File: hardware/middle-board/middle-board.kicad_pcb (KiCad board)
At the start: 4 copper layers, 39 x 110 mm, 69 parts, among them J1 Conn_01x10_Socket, J2 Conn_01x15_Socket, J3 Conn_01x10_Pin, J4 Conn_01x09_Socket, J5 Conn_01x09_Socket, J6 Conn_01x12_Pin, Q1 2N3904, Q2 2N3906, Q3 2N3904, Q4 2N3906, U1 TL084, U2 TL074, U3 TL072, U4 NE5517

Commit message: wip - first pass done
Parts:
- C10, C3, C4, C5, C6, C7, C8, C9: footprint Capacitor_THT:C_Disc_D3.4mm_W2.1mm_P2.50mm -> Eurorack Common:C_Disc_D3.4mm_W2.1mm_P2.50mm
- Q1, Q2, Q3, Q4: footprint Package_TO_SOT_THT:TO-92_Inline -> Eurorack Common:TO-92_Inline
- R1, R10, R11, R12, R13, R14, R15, R16, R17, R18, R19, R2, R20, R21, R22, R23, R24, R25, R26, R27, R28, R29, R3, R30, R31, R32, R33, R34, R35, R36, R37, R38, R39, R4, R40, R41, R42, R43, R5, R6, R7, R8, R9: footprint Resistor_THT:R_Axial_DIN0207_L6.3mm_D2.5mm_P7.62mm_Horizontal -> Eurorack Common:R_Axial_DIN0207_L6.3mm_D2.5mm_P7.62mm_Horizontal
- U2: footprint Package_DIP:DIP-14_W7.62mm -> Eurorack Common:DIP-14_W7.62mm
- U3: footprint Package_DIP:DIP-8_W7.62mm -> Eurorack Common:DIP-8_W7.62mm
- U4: footprint Package_SO:JEITA_SOIC-16_3.9x9.9mm_P1.27mm -> Eurorack Common:SOIC-16_3.9x9.9mm_P1.27mm

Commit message: chore: clean up the boards
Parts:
- J1: value Conn_01x10_Socket -> 01x10 Male Pin Header
- J2: value Conn_01x15_Socket -> 01x13 Female Pin Header
- J3: value Conn_01x10_Pin -> 01x10 Male Pin Header
- J4, J5: value Conn_01x09_Socket -> 01x09 Female Pin Header
- J6: value Conn_01x12_Pin -> 01x12 Female Pin Header
- RV1, RV3: value 2K -> B2K
- RV2, RV4: value 100K -> B100K

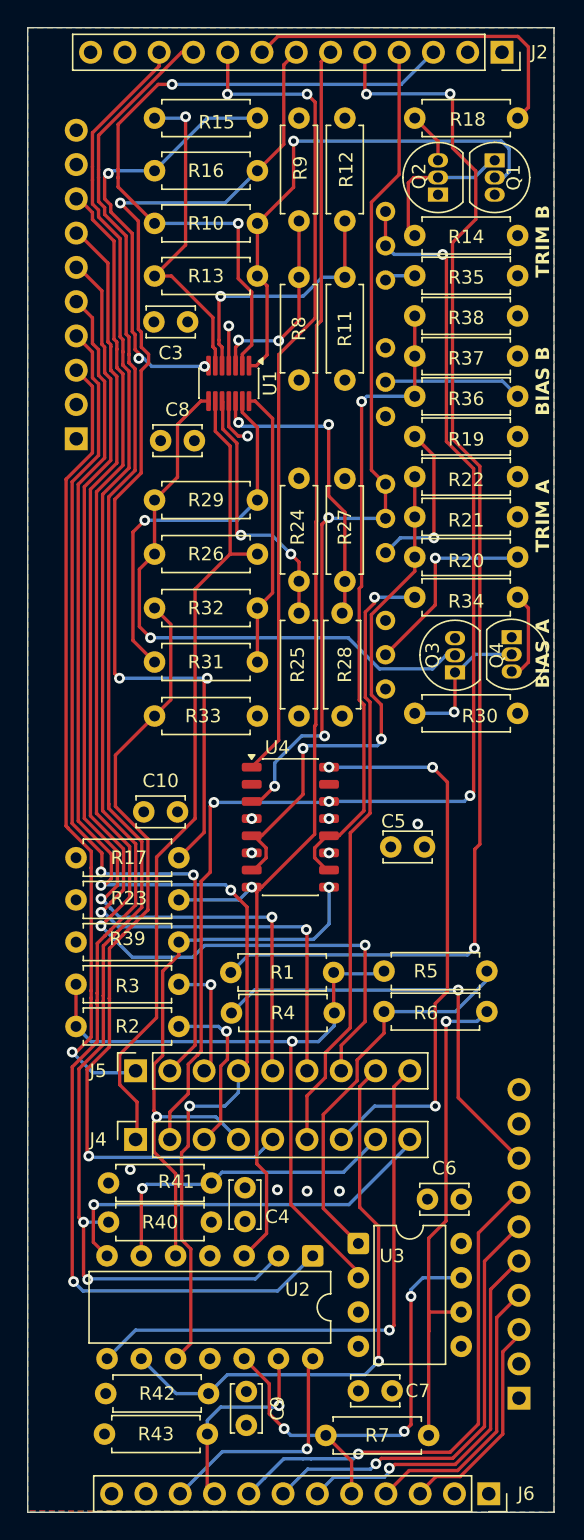
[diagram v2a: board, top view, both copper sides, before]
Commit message: feature: optional DIP footprint on PCB for TL0X4 op amps
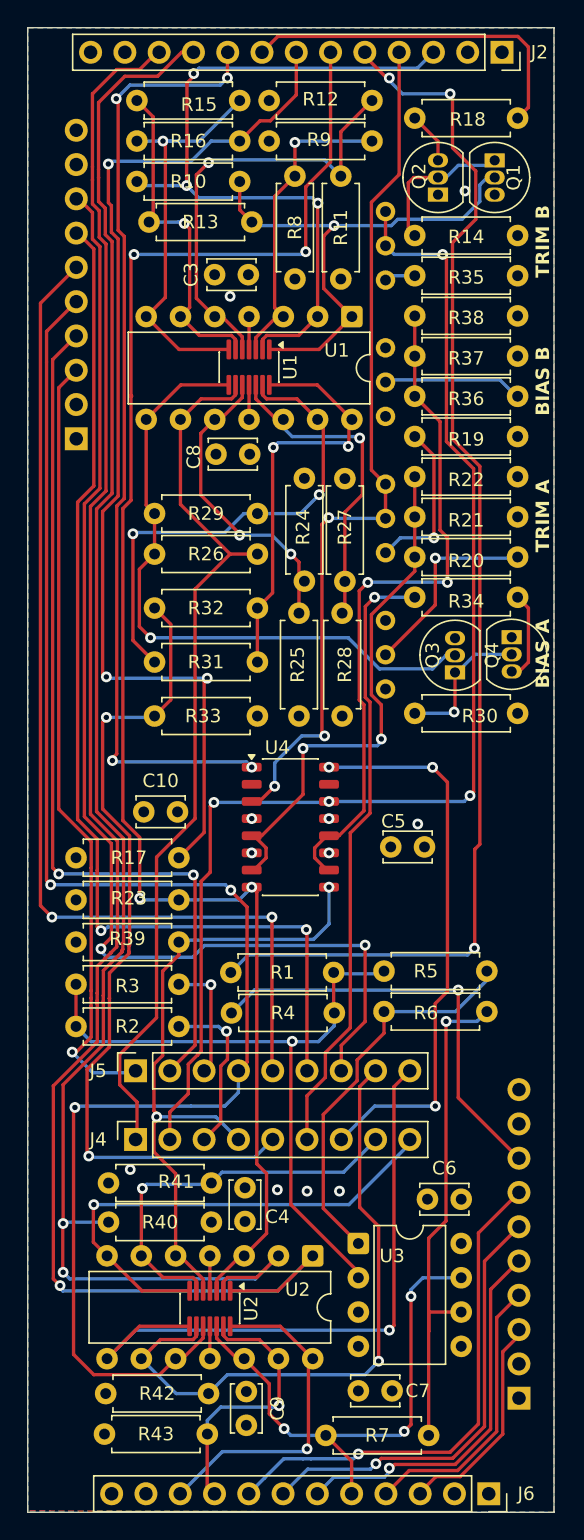
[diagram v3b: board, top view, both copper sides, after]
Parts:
- added U1: TL084, Eurorack Common:DIP-14_W7.62mm, F.Cu at (44.0, 41.4)
- added U2: TL074, Eurorack Common:Texas_DYY0014A_TSOT-23-14_2x4.2mm_P0.5mm, F.Cu at (33.5, 114.9)
- moved R9 8.02 mm to (45.5, 28.4), turned to 180 degrees
- moved R11 7.50 mm to (43.2, 31.0)
- moved R8 7.50 mm to (39.8, 38.6)
- moved R12 5.76 mm to (37.9, 25.4), turned to 0 degrees
- moved C3 5.70 mm to (36.4, 38.3)
- moved C8 4.22 mm to (34.0, 51.6)
- moved R13 4.02 mm to (36.6, 34.4)
- moved R10 3.37 mm to (28.1, 31.4)
- moved R16 2.56 mm to (28.1, 28.4)
- moved U1 1.92 mm to (36.4, 45.2)
- moved R15 1.85 mm to (35.7, 25.4)
- moved R29 1.00 mm to (29.4, 56.0)
- moved R24 0.40 mm to (40.5, 53.4)
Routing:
- net /OUT_C: track 95.7 -> 116.6 mm
- net /OUT_A: track 99.0 -> 117.7 mm, vias 1 -> 4
- net Net-(U1B-+): track 19.2 -> 32.9 mm
- net Net-(R31-Pad1): track 20.8 -> 31.5 mm, vias 0 -> 2
- net /COMMON_A: track 61.1 -> 71.0 mm, vias 2 -> 4
- net /LED_A2: track 117.2 -> 125.7 mm
- net Net-(U1D--): track 28.3 -> 36.6 mm, vias 1 -> 2
- net /LED_A1: track 116.4 -> 124.7 mm
- net Net-(U1A-+): track 15.2 -> 23.1 mm, vias 2 -> 1
- net /LED_B2: track 29.8 -> 37.0 mm
- net /LED_C2: track 41.6 -> 48.8 mm
- net /LED_MIX2: track 17.6 -> 24.7 mm
- net /LED_B1: track 23.8 -> 29.4 mm
- net /LED_C1: track 42.2 -> 47.7 mm
- net /LED_MIX1: track 14.9 -> 20.4 mm
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
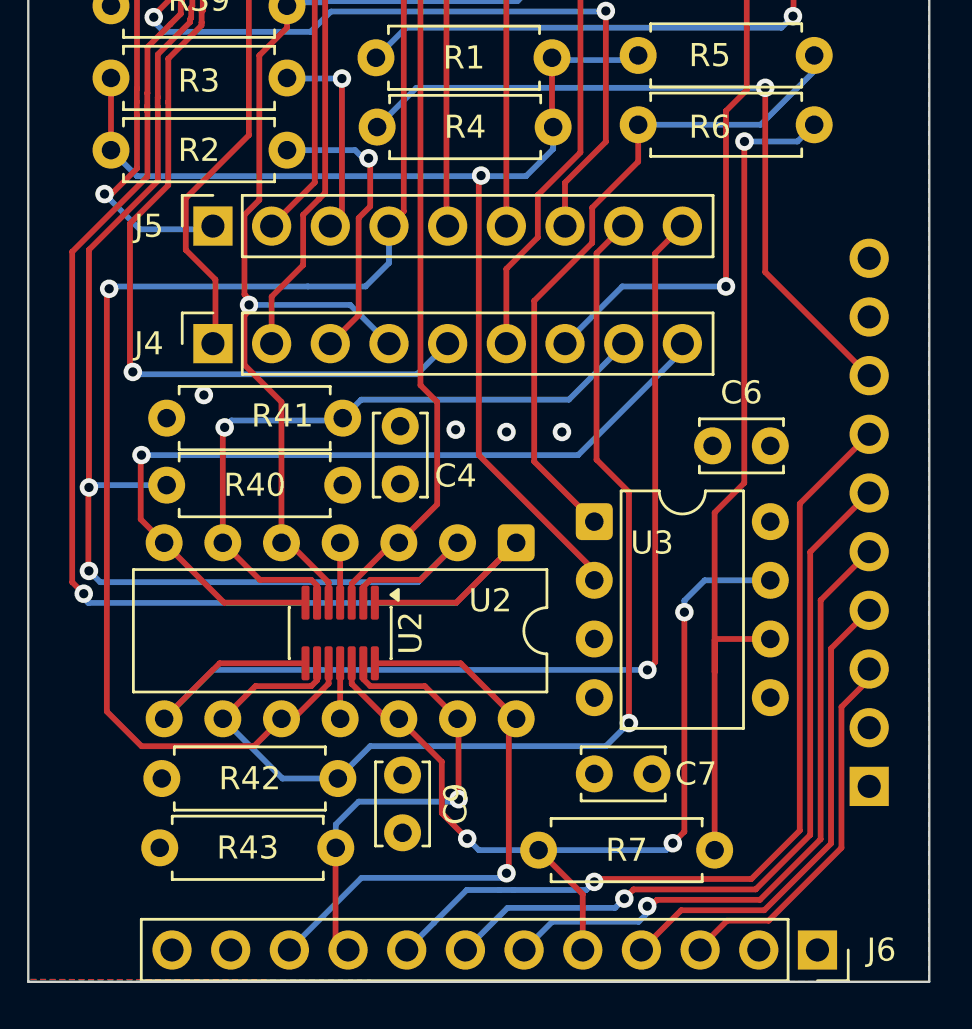
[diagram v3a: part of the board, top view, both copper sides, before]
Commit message: fix: inverted power pins on op amps
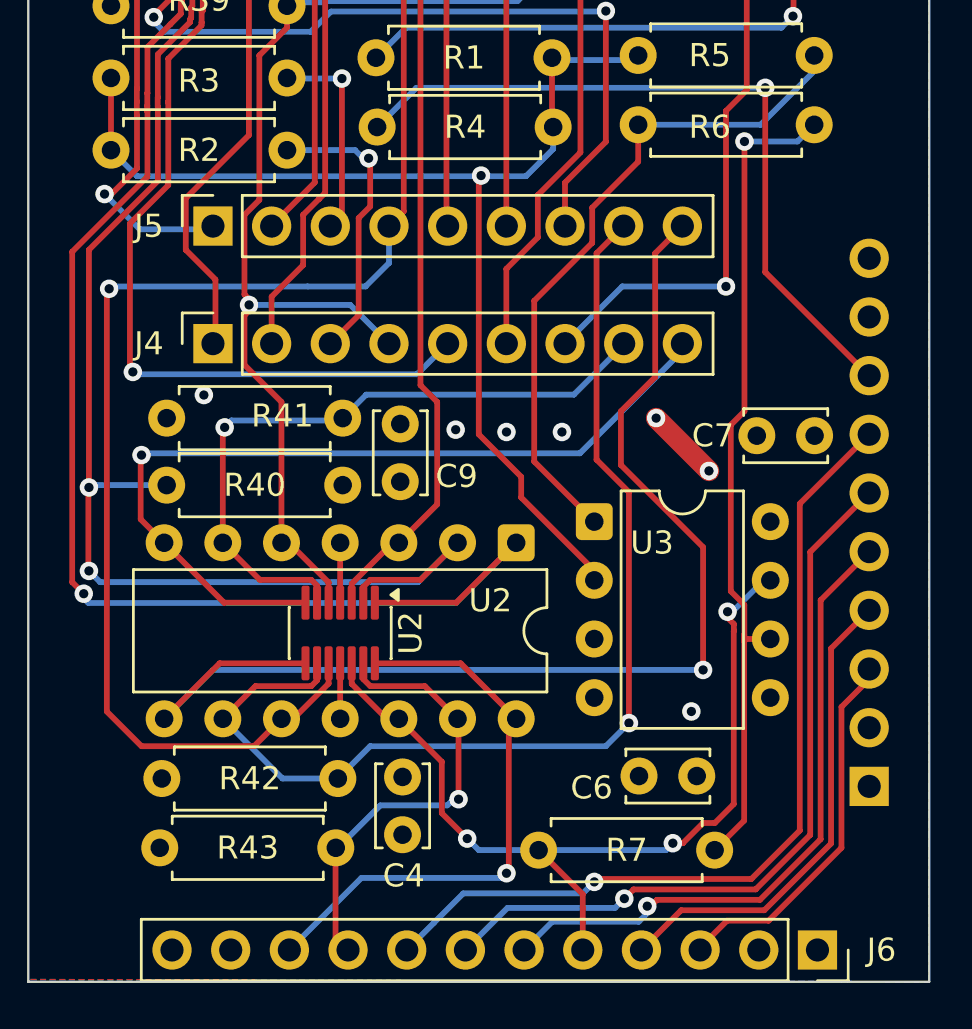
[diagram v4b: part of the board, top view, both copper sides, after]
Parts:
- moved C7 17.5 mm to (54.0, 106.4), turned to 180 degrees
- moved C6 14.3 mm to (48.9, 121.1), turned to 180 degrees
- moved C4 2.58 mm to (36.2, 123.6), turned to 90 degrees
- moved C9 2.40 mm to (36.1, 108.4), turned to 90 degrees
- renumbered C9 to C4, C4 to C9
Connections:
- C4 pad 1: +12V -> GND
- C4 pad 2: GND -> -12V
- C9 pad 1: GND -> +12V
- C9 pad 2: -12V -> GND
- U2 pad 11: +12V -> -12V (x2)
- U2 pad 4: -12V -> +12V (x2)
- U3 pad 4: +12V -> -12V
- U3 pad 8: -12V -> +12V
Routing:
- net -12V: track 88.0 -> 100.5 mm
- net /LED_C2: track 48.8 -> 53.1 mm
- net Net-(U3B--): track 38.3 -> 36.4 mm
- net +12V: track 42.0 -> 41.4 mm, vias 1 -> 3
- net /MIX_OUT: track 39.1 -> 38.5 mm
- net /LED_MIX1: track 20.4 -> 19.8 mm
- net GND: vias 9 -> 10
